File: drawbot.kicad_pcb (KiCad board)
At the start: 2 copper layers, 148.4 x 81.9 mm, 35 parts, among them J1 24v (motors), J2 24v (laser), J3 24v (everything else), J4 OLED Display, J5 E Stop, T1 Stepper Driver (X-Axis), T2 Stepper Driver (Y-Axis), T3 Stepper Driver (Z-Axis)

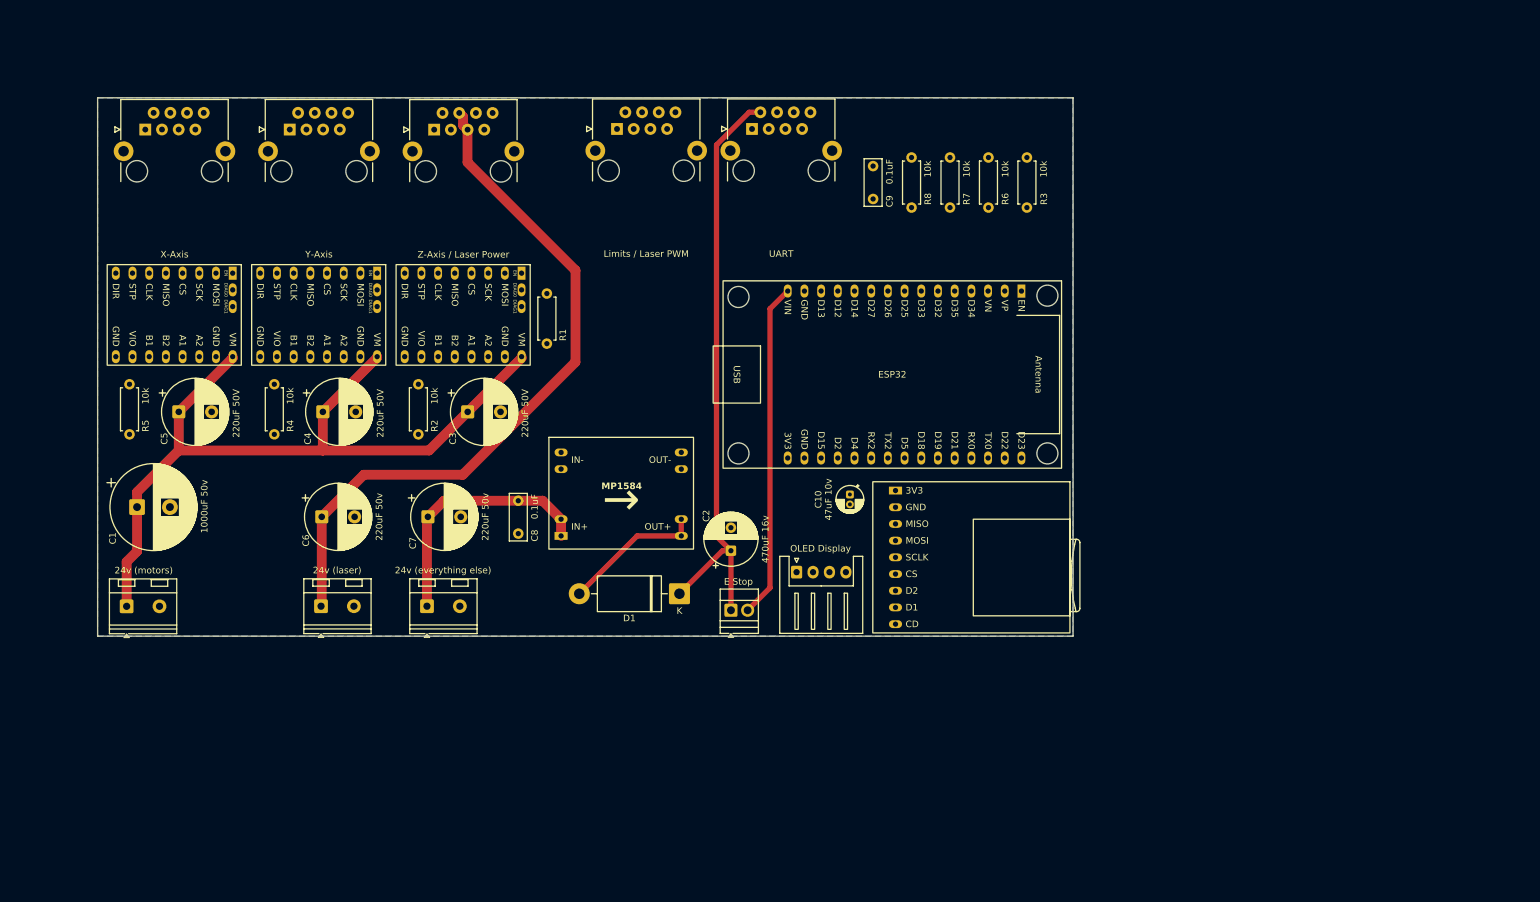
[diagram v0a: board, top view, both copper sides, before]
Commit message: rearrange and connect everything
rearrange and connect everything
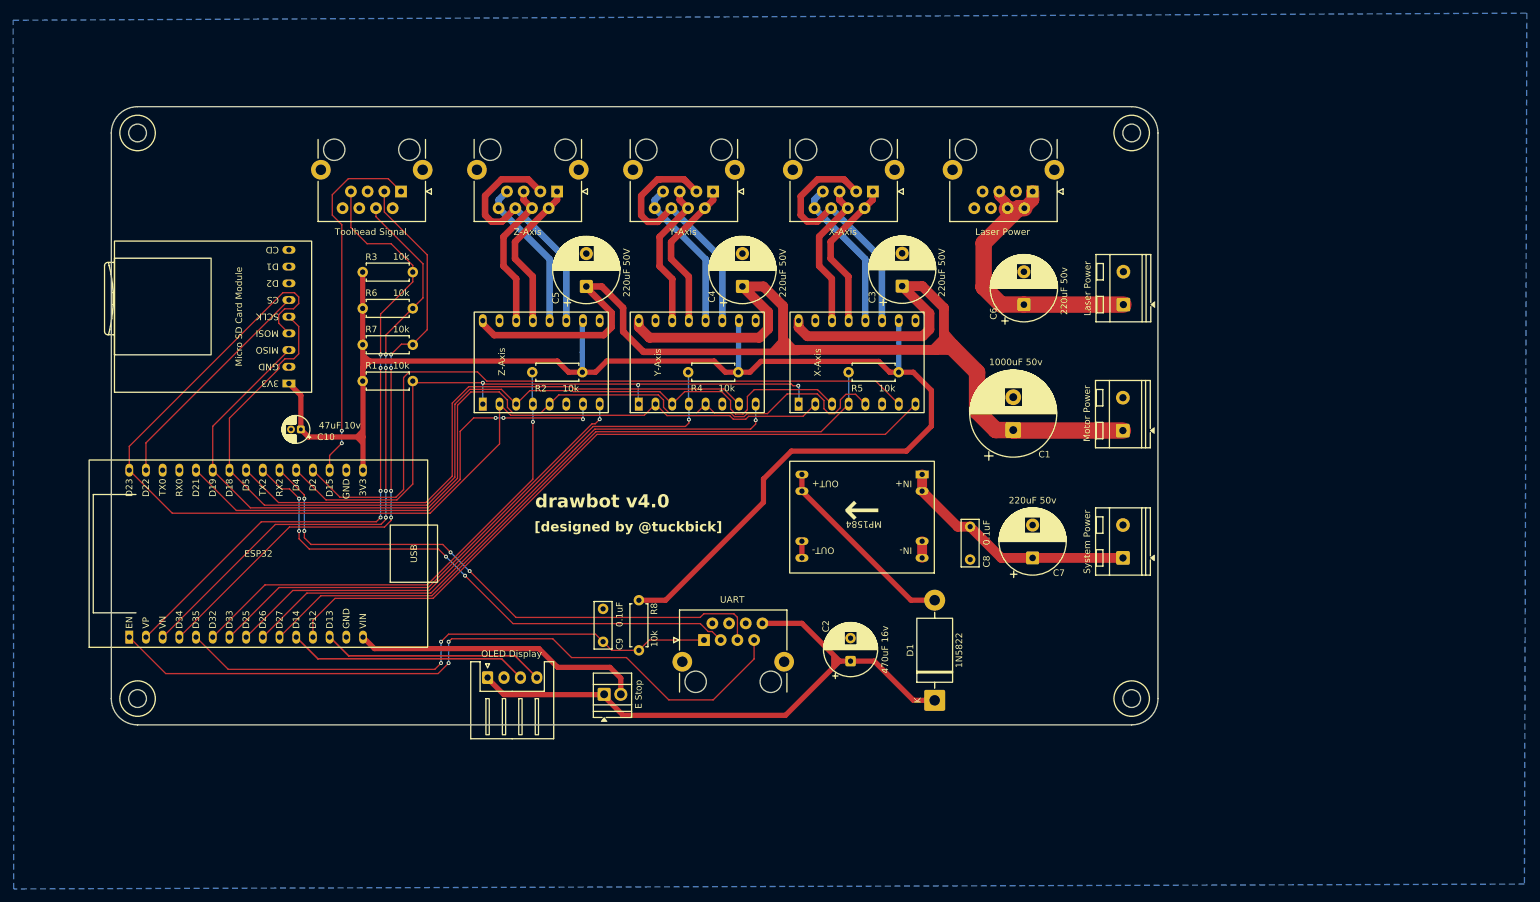
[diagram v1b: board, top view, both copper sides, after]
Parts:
- added N6: UART, Connector_RJ:RJ45_HALO_HFJ11-x2450HRL_Horizontal, F.Cu at (123.3, 109.2)
- added REF**: MountingHole_2.7mm, MountingHole:MountingHole_2.7mm, F.Cu at (37.1, 118.1)
- added REF**: MountingHole_2.7mm, MountingHole:MountingHole_2.7mm, F.Cu at (37.1, 32.0)
- added REF**: MountingHole_2.7mm, MountingHole:MountingHole_2.7mm, F.Cu at (188.3, 118.1)
- added REF**: MountingHole_2.7mm, MountingHole:MountingHole_2.7mm, F.Cu at (188.3, 32.0)
- J1: value 24v (motors) -> Motor Power
- J2: value 24v (laser) -> Laser Power
- J3: value 24v (everything else) -> System Power
- N3: value Z-Axis / Laser Power -> Z-Axis
- N4: value Limits / Laser PWM -> Laser Power
- N5: value UART -> Toolhead Signal
- T1: value Stepper Driver (X-Axis) -> X-Axis; footprint mine:TMC5160 -> mine:TMC5160_1
- T2: value Stepper Driver (Y-Axis) -> Y-Axis; footprint mine:TMC5160 -> mine:TMC5160_1
- T3: value Stepper Driver (Z-Axis) -> Z-Axis; footprint mine:TMC5160 -> mine:TMC5160_1
- moved J1 153.9 mm to (187.0, 77.3), turned to 90 degrees
- moved E1 139.0 mm to (38.2, 105.7), turned to 90 degrees
- moved C1 133.8 mm to (170.3, 77.2), turned to 90 degrees
- moved J2 130.4 mm to (187.1, 58.2), turned to 90 degrees
- moved SD1 125.4 mm to (46.5, 59.3), turned to 90 degrees
- moved C6 111.6 mm to (171.9, 58.2), turned to 90 degrees
- moved N1 111.1 mm to (149.0, 41.0), turned to 180 degrees
- moved R5 109.8 mm to (145.2, 68.5), turned to 0 degrees
- moved J3 106.1 mm to (187.0, 96.7), turned to 90 degrees
- moved T1 104.1 mm to (146.5, 67.0), turned to 90 degrees
- moved R3 93.9 mm to (79.0, 53.2), turned to 180 degrees
- moved C7 92.2 mm to (173.2, 96.7), turned to 90 degrees
- moved R6 88.9 mm to (79.0, 58.7), turned to 180 degrees
- moved R7 84.4 mm to (79.0, 64.3), turned to 180 degrees
- moved C10 84.1 mm to (61.9, 77.2), turned to 180 degrees
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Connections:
- net +24V_MOTORS renamed +MOTOR_PWR
- net X_A1 renamed X_A+
- net X_A2 renamed X_A-
- net X_B1 renamed X_B+
- net X_B2 renamed X_B-
- net Y_A1 renamed Y_A+
- net Y_A2 renamed Y_A-
- net Y_B1 renamed Y_B+
- net Y_B2 renamed Y_B-
- C6 pad 1: +24V_LASER -> +LASER_PWR
- E1 pad 10: Y_CS -> X_CS
- E1 pad 11: X_DIR -> I2C_SCL
- E1 pad 12: Z_STEP -> X_DIR
- E1 pad 13: X_CS -> I2C_SDA
- E1 pad 18: MOT_EN -> LASER_PWM
- E1 pad 2: GPIO_AUX -> X_LIMIT
- E1 pad 20: Z_CS -> MOT_EN
- E1 pad 23: SD_CS -> Y_STEP
- E1 pad 26: I2C_SDA -> Z_STEP
- E1 pad 29: I2C_SCL -> SD_CS
- E1 pad 4: X_LIMIT -> Y_LIMIT
- E1 pad 5: Y_LIMIT -> GPIO_AUX
- E1 pad 6: Z_DIR -> Z_CS
- E1 pad 7: LASER_PWM -> Z_DIR
- E1 pad 8: Y_DIR -> Y_CS
- E1 pad 9: Y_STEP -> Y_DIR
- J2 pad 1: +24V_LASER -> +LASER_PWR
- J4 pad 1: +3.3V -> +5V
- N3 pad 1: Z_A1 -> Z_A+
- N3 pad 2: Z_B1 -> Z_A+
- N3 pad 3: Z_A2 -> Z_B+
- N3 pad 4: +24V_LASER -> Z_A-
- N3 pad 5: +24V_LASER -> Z_A-
- N3 pad 6: Z_B2 -> Z_B+
- N3 pad 7: GND -> Z_B-
- N3 pad 8: GND -> Z_B-
- N4 pad 1: LASER_PWM -> +LASER_PWR
- N4 pad 2: GND -> +LASER_PWR
- N4 pad 3: Y_LIMIT -> GND
- N4 pad 4: Z_PROBE -> +LASER_PWR
- N4 pad 5: GND -> +LASER_PWR
- N4 pad 7: X_LIMIT -> GND
- N5 pad 1: ESP_EN -> LASER_PWM
- N5 pad 2: +5V -> GND
- N5 pad 3: UART_TX -> Y_LIMIT
- N5 pad 4: GND -> Z_PROBE
- N5 pad 5: UART_RX -> GND
- N5 pad 7: GPIO_AUX -> X_LIMIT
- R3 pad 1: GPIO_AUX -> X_LIMIT
- R7 pad 1: X_LIMIT -> Y_LIMIT
- R8 pad 1: Y_LIMIT -> GPIO_AUX
- T3 pad 11: Z_B1 -> Z_B+
- T3 pad 12: Z_B2 -> Z_B-
- T3 pad 13: Z_A1 -> Z_A+
- T3 pad 14: Z_A2 -> Z_A-
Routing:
- net +3.3V: track 0.00 -> 227.5 mm
- net SPI_MOSI: track 0.00 -> 168.4 mm
- net SPI_MISO: track 0.00 -> 150.7 mm
- net SPI_SCK: track 0.00 -> 146.0 mm
- net ESP_EN: track 0.00 -> 110.8 mm, vias 0 -> 2
- net X_STEP: track 0.00 -> 110.8 mm
- net X_DIR: track 0.00 -> 107.9 mm
- net +24V_LASER: track 107.2 -> 0.00 mm
- net X_CS: track 0.00 -> 106.1 mm
- net MOT_EN: track 0.00 -> 104.5 mm, vias 0 -> 3
- net X_LIMIT: track 0.00 -> 100.9 mm, vias 0 -> 4
- net Y_LIMIT: track 0.00 -> 95.6 mm, vias 0 -> 4
- net Z_PROBE: track 0.00 -> 94.5 mm, vias 0 -> 4
- net +MOTOR_PWR: track 120.5 -> 214.4 mm
- net Y_STEP: track 0.00 -> 91.9 mm
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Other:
- board size 148.4 x 81.9 mm -> 159.2 x 94 mm
- board text added: "D15"
- board text added: "[designed by @tuckbick]"
- board text added: "drawbot v4.0"
